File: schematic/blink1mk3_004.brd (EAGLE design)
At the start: 13.2 x 13.7 mm, 14 parts, among them U1 EFM32HG309F64G, X1 USB

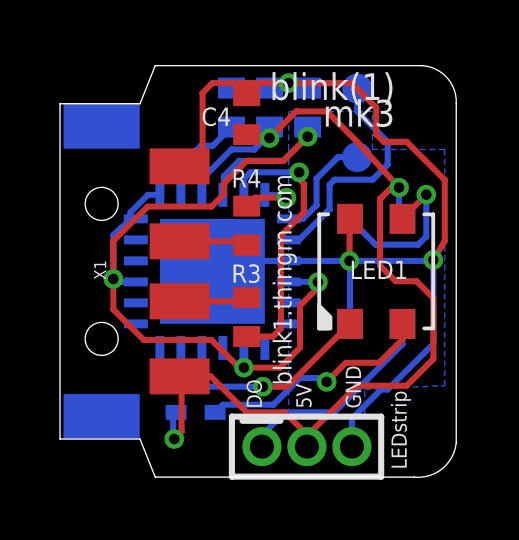
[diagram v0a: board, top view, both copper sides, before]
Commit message: fix EFM32HG309 pad spacing issue. omg what a slog
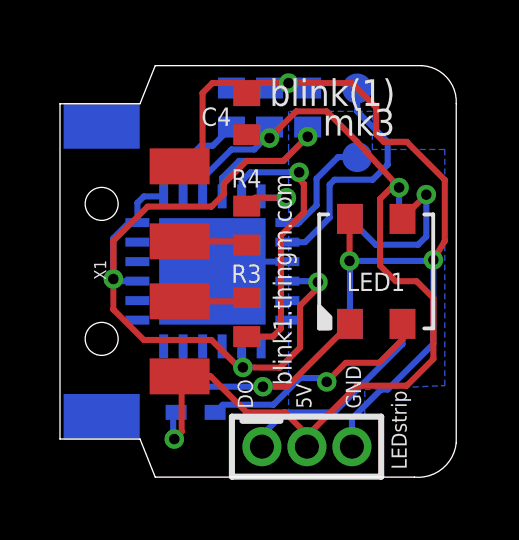
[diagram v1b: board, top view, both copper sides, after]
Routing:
- net GND: track 39.5 -> 37.3 mm
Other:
- board text added: "blink1mk3_004B"
- board text removed: "blink1mk3_004"
